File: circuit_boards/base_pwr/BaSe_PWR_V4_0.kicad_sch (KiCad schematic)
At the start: 105 parts, among them J1 12VDC In, J1 USB_C_Receptacle, J11 Conn_01x07_Pin, J2 USB_B_Micro, J3 USB3_A, J4 Screw_Terminal_01x04, J5 MOTOR, J5 Screw_Terminal_01x03, J7 USB3_B_Micro, P1 USB_C_Plug, Q2 BSS214NW, Q3 BSS214NW, Q4 BSS214NW, Q5 BSS214NW, U2 AMS1117-3.3, U3 STM32F070RBTx, U4 LM2596S-5, U5 DRV8220, U6 AMS1117-3.3, Y1 32.768kHz, Y2 8MHz

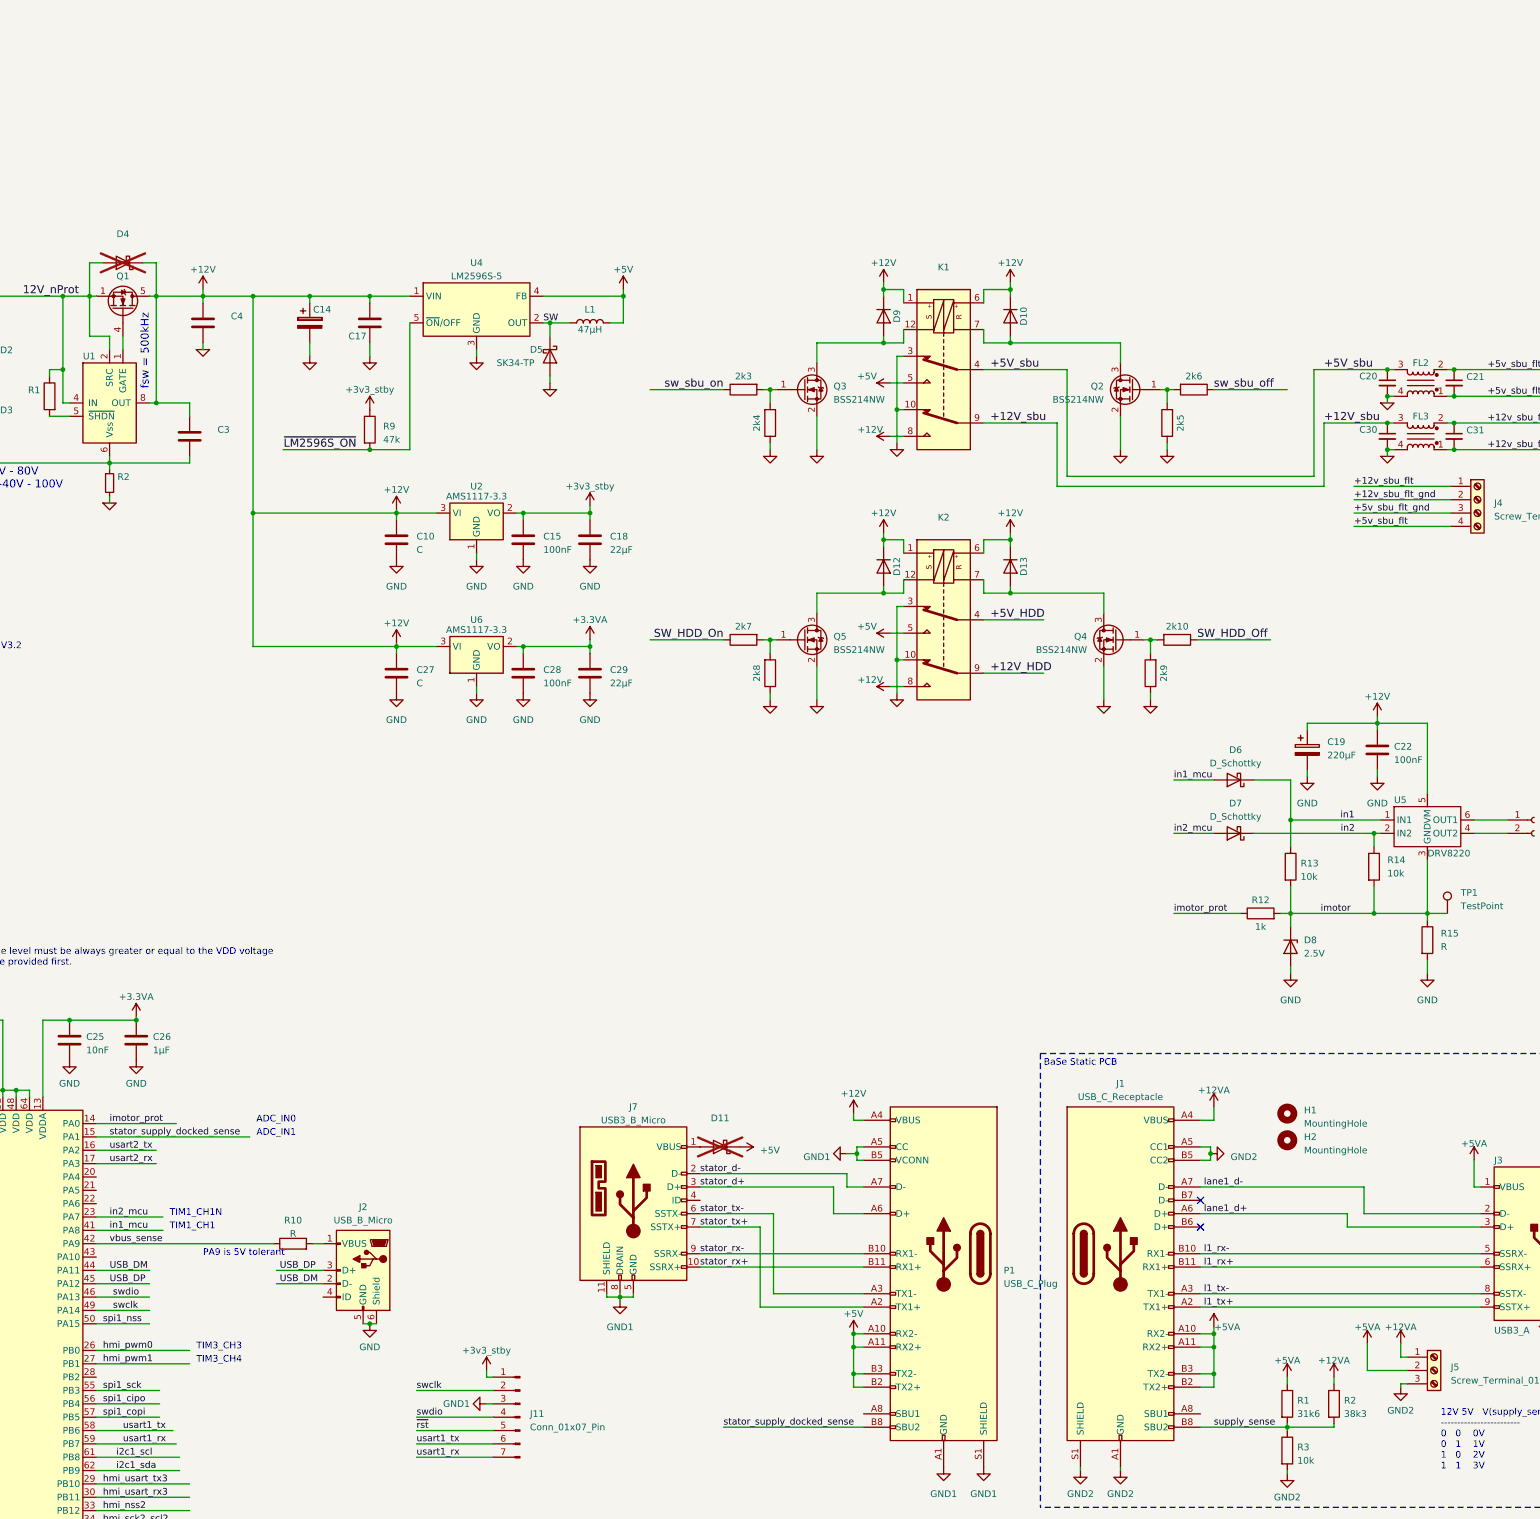
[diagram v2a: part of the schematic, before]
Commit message: BaSe PWR V4.0: more layout sketches
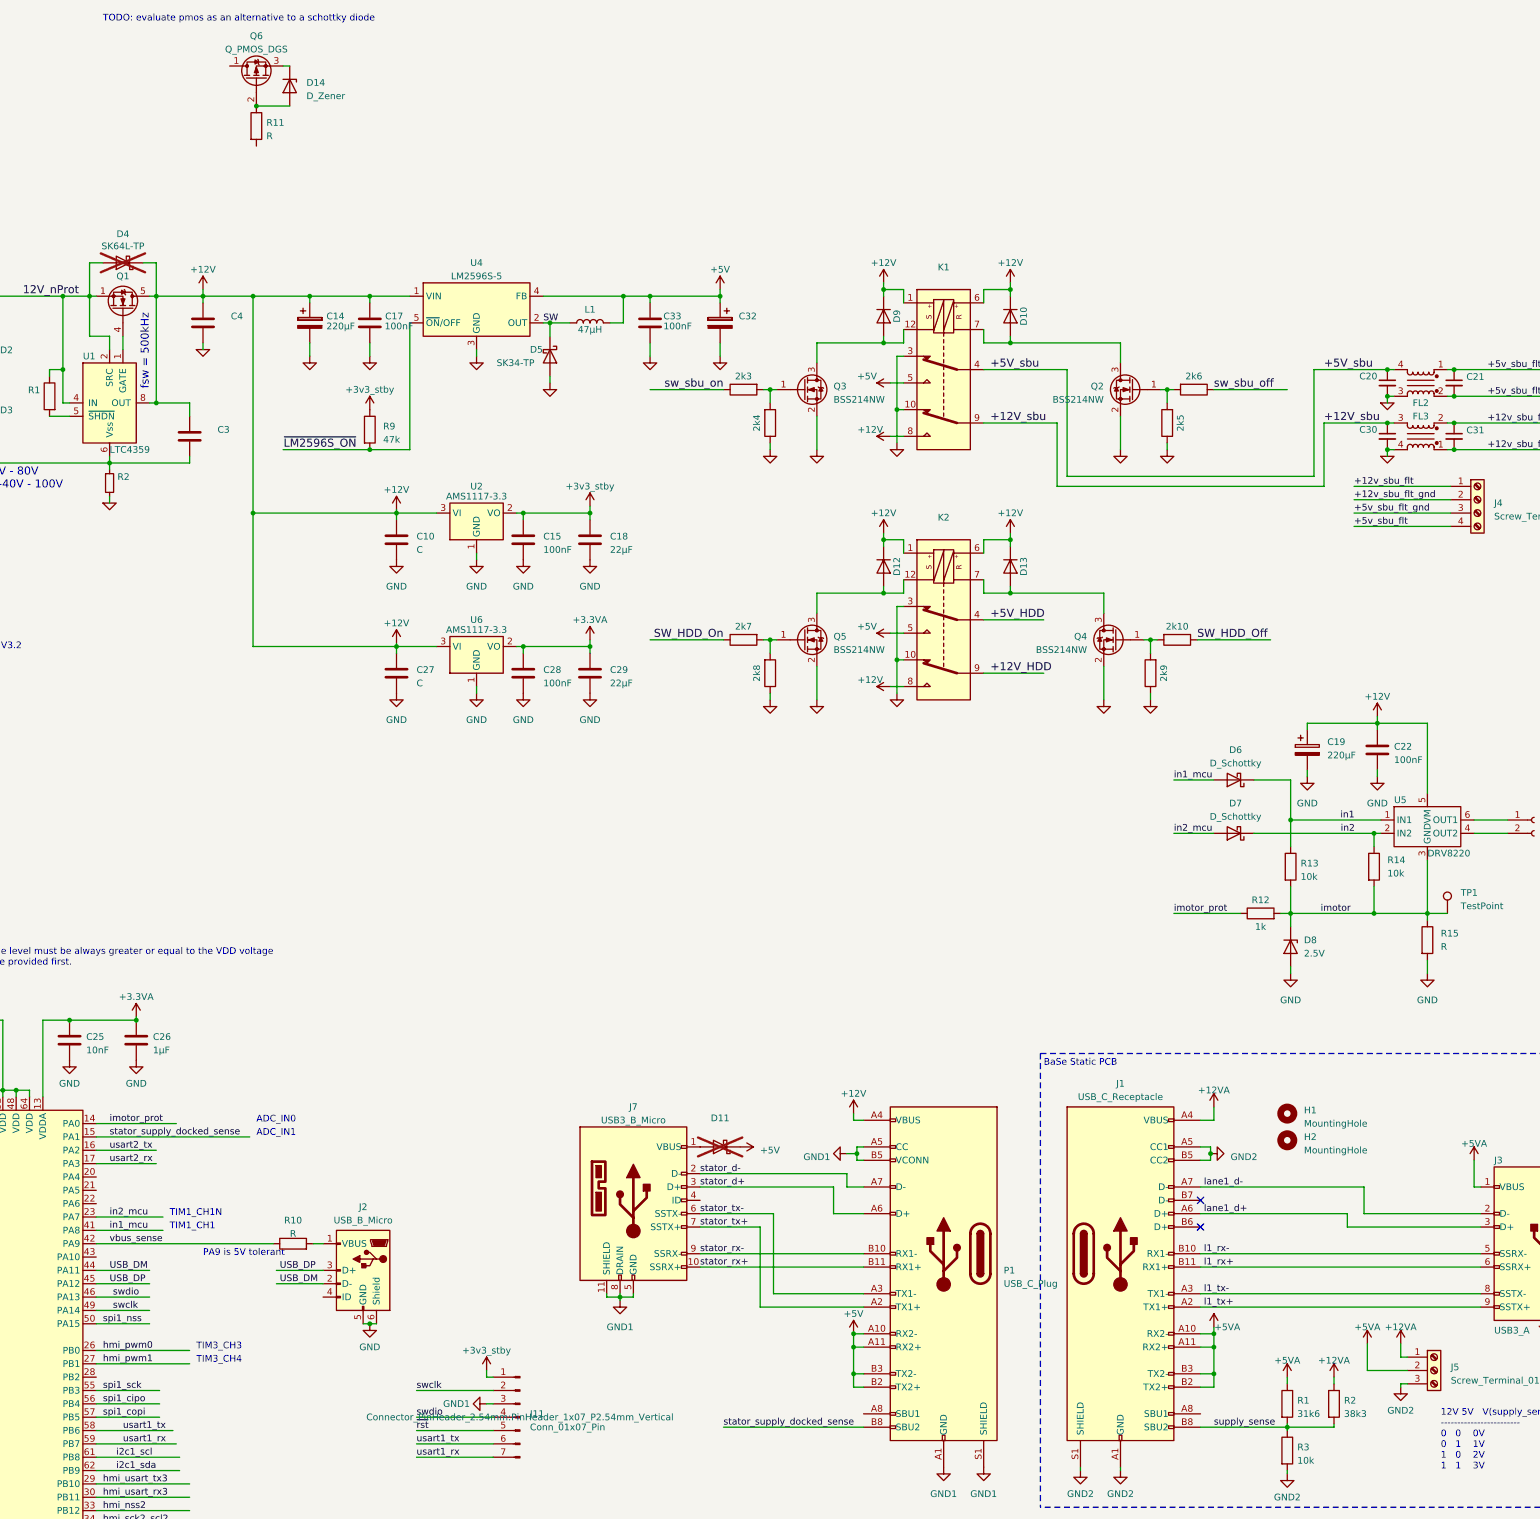
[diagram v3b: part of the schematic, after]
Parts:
- added C32: ~, Capacitor_SMD:C_0603_1608Metric_Pad1.08x0.95mm_HandSolder, symbol Waberinator_rev1-rescue:CP
- added C33: 100nF, Capacitor_SMD:C_0603_1608Metric_Pad1.08x0.95mm_HandSolder, symbol Waberinator_rev1-rescue:C
- added D14: D_Zener, symbol Device:D_Zener
- added Q6: Q_PMOS_DGS, symbol Device:Q_PMOS_DGS
- added R11: R, symbol Device:R
- C14: value ~ -> 220µF
- C17: value ~ -> 100nF
- D1: footprint (none) -> Diode_SMD:D_SOD-128
- D4: value ~ -> SK64L-TP
- F1: footprint (none) -> Fuse:Fuse_2512_6332Metric_Pad1.52x3.35mm_HandSolder; SPN F3147CT-ND -> (none); digikey (none) -> F3147CT-ND
- J1: footprint (none) -> Connector_JST:JST_XA_S02B-XASK-1N-BN_1x02_P2.50mm_Horizontal
- J11: footprint (none) -> Connector_PinHeader_2.54mm:PinHeader_1x07_P2.54mm_Vertical
- U1: value ~ -> LTC4359
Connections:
- net +5V: now also C32.1, C33.2
- net +5V_sbu: now also FL2.4; no longer FL2.3
- net +5v_sbu_flt: now also FL2.1; no longer FL2.2
- net +5v_sbu_flt_gnd: now also FL2.2; no longer FL2.1
- net GND: now also FL2.3, C32.2, C33.1; no longer FL2.4
- new net: D14.1 (K), Q6.3 (S)
- new net: D14.2 (A), Q6.2 (G), R11.1
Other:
- note added: "TODO: evaluate pmos as an alternative to a schottky diode"
- moved on the sheet: FL2

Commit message: BaSe PWR V4.0: design reverse polarity protection
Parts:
- removed C3, C4: ~, Capacitor_SMD:C_0603_1608Metric_Pad1.08x0.95mm_HandSolder, symbol BackupServer-rescue:C-BackupServer-rescue
- removed C32: ~, Capacitor_SMD:C_0603_1608Metric_Pad1.08x0.95mm_HandSolder, symbol Waberinator_rev1-rescue:CP
- removed D2, D3: ~, symbol Device:D_Zener
- removed D4: SK64L-TP, symbol Device:D_Schottky
- removed Q1: ~, symbol Transistor_FET:BSC028N06LS3
- removed R1: ~, Resistor_SMD:R_0603_1608Metric_Pad0.98x0.95mm_HandSolder, symbol BackupServer-rescue:R-BackupServer-rescue
- removed R2: ~, Resistor_SMD:R_0603_1608Metric_Pad0.98x0.95mm_HandSolder, symbol Device:R_Small
- removed U1: LTC4359, symbol Power_Management:LTC4359-MS8
- added C3: 220µF, Capacitor_SMD:C_Elec_10x10.2, symbol Waberinator_rev1-rescue:CP
- added R1: 100k, symbol Device:R
- C14: footprint Capacitor_SMD:C_0603_1608Metric_Pad1.08x0.95mm_HandSolder -> Capacitor_SMD:C_Elec_10x10.2
- C19: footprint Capacitor_SMD:C_Elec_6.3x7.7 -> Capacitor_SMD:C_Elec_10x10.2
- D1: value ~ -> 824501121
- D14: now not fitted
- J5: footprint Connector_PinHeader_2.54mm:PinHeader_1x02_P2.54mm_Vertical -> Connector_JST:JST_XA_S02B-XASK-1N-BN_1x02_P2.50mm_Horizontal
- Q6: value Q_PMOS_DGS -> AOSP21321; footprint (none) -> Package_SO:SO-8_3.9x4.9mm_P1.27mm
- R11: value R -> 100
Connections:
- net +12V: now also D14.1 (K), Q6.1 (S), Q6.2 (S), Q6.3 (S), R1.1
- net +3V3_STBY: no longer R9.1
- net +5V: now also C3.1
- net 12V_nProt: now also Q6.5 (D), Q6.6 (D), Q6.7 (D), Q6.8 (D)
- net GND: now also R11.2, R9.2, C3.2
- net ~{LM2596S_ON}: now also R9.1; no longer R9.2
- net at D14.2 (A), R11.1: now also Q6.4 (G), R1.2; no longer Q6.2 (G)
- net at U5.4 (OUT2): now also J5.1 (Pin_1); no longer J5.2 (Pin_2)
- net at U5.6 (OUT1): now also J5.2 (Pin_2); no longer J5.1 (Pin_1)
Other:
- note added: "5A flow at about 16V"
- note removed: "Operating: 4V - 80V Withstands: -40V - 100V"
- note removed: "TODO: evaluate pmos as an alternative to a schottky diode"
- note removed: "fsw = 500kHz"
- moved on the sheet: C1, C2, D1, FL1, J1, R11, R9

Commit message: BaSe PWR V4.0: settle on rough component distribution
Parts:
- removed C20, C21, C30, C31: ~, Capacitor_SMD:C_0603_1608Metric_Pad1.08x0.95mm_HandSolder, symbol Device:C_Small
- removed FL2, FL3: ~, g7_emi:CMC_Laird_CM2021Y330R-10, symbol Device:EMI_Filter_LL_1423
- removed J4: Screw_Terminal_01x04, TerminalBlock_Phoenix:TerminalBlock_Phoenix_MKDS-1,5-4_1x04_P5.00mm_Horizontal, symbol Connector:Screw_Terminal_01x04
- added J10: Conn_01x04_Socket, Connector_JST:JST_XH_B4B-XH-A_1x04_P2.50mm_Vertical, symbol Connector:Conn_01x04_Socket
- J1, J5: footprint Connector_JST:JST_XA_S02B-XASK-1N-BN_1x02_P2.50mm_Horizontal -> Connector_JST:JST_XH_B2B-XH-A_1x02_P2.50mm_Vertical
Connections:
- net +12V_sbu: now also J10.1 (Pin_1)
- net +5V_sbu: now also J10.4 (Pin_4)
- net GND: now also J10.2 (Pin_2), J10.3 (Pin_3)
- net USB_DM renamed USB_D-
- net USB_DP renamed USB_D+

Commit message: BaSe PWR V4.0: split pcbs so all connectors can face far end.
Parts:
- removed C7, C8: 4.3pF, Capacitor_SMD:C_0603_1608Metric_Pad1.08x0.95mm_HandSolder, symbol Device:C
- removed J5: Screw_Terminal_01x03, TerminalBlock_Phoenix:TerminalBlock_Phoenix_MKDS-1,5-3_1x03_P5.00mm_Horizontal, symbol Connector:Screw_Terminal_01x03
- removed R4: R, Resistor_SMD:R_0603_1608Metric_Pad0.98x0.95mm_HandSolder, symbol Device:R
- removed Y1: 32.768kHz, Crystal:Crystal_SMD_Abracon_ABS25-4Pin_8.0x3.8mm, symbol Device:Crystal
- added H1, H2: MountingHole, MountingHole:MountingHole_2.7mm_M2.5_DIN965, symbol Mechanical:MountingHole
- added J12: Conn_02x06_Odd_Even, Connector_PinHeader_2.54mm:PinHeader_2x06_P2.54mm_Vertical, symbol Connector_Generic:Conn_02x06_Odd_Even
- added J13: Conn_01x04_Socket, Connector_JST:JST_XH_B4B-XH-A_1x04_P2.50mm_Vertical, symbol Connector:Conn_01x04_Socket
- added J4: Conn_02x06_Odd_Even, Connector_PinSocket_2.54mm:PinSocket_2x06_P2.54mm_Vertical, symbol Connector_Generic:Conn_02x06_Odd_Even
- C10, C27: value C -> 100nF
- H1, H2: footprint MountingHole:MountingHole_3.2mm_M3_DIN965 -> MountingHole:MountingHole_2.7mm_M2.5_DIN965
- R1, R11: footprint (none) -> Resistor_SMD:R_0603_1608Metric_Pad0.98x0.95mm_HandSolder
- R6: value 33k -> 24,9k
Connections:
- net +12V: no longer P1.A4 (VBUS), P1.A9 (VBUS), P1.B4 (VBUS), P1.B9 (VBUS)
- net +12VA: now also J13.4 (Pin_4)
- net +12V_HDD: now also J4.5 (Pin_5), J4.6 (Pin_6)
- net +12V_sbu: now also J10.4 (Pin_4); no longer J10.1 (Pin_1)
- net +3V3_STBY: now also J4.12 (Pin_12)
- net +5V: no longer D11.1 (K), P1.A10 (RX2-), P1.A11 (RX2+), P1.B2 (TX2+), P1.B3 (TX2-)
- net +5VA: now also J13.1 (Pin_1)
- net +5V_HDD: now also J4.3 (Pin_3), J4.4 (Pin_4)
- net +5V_sbu: now also J10.1 (Pin_1); no longer J10.4 (Pin_4)
- net GND: now also J4.1 (Pin_1), J4.2 (Pin_2), J4.7 (Pin_7), J4.8 (Pin_8)
- net GND1: now also J12.1 (Pin_1), J12.2 (Pin_2), J12.7 (Pin_7), J12.8 (Pin_8); no longer P1.A5 (CC), P1.B5 (VCONN)
- net GND2: now also J13.2 (Pin_2), J13.3 (Pin_3); no longer J1.A5 (CC1), J1.B5 (CC2)
- net i2c1_scl: now also J4.9 (Pin_9)
- net i2c1_sda: now also J4.10 (Pin_10)
- net supply_sense: now also J1.A5 (CC1); no longer J1.B8 (SBU2)
- net aux_i2c_scl: now reaches P1.A8 (SBU1)
- net stator_supply_docked_sense renamed aux_i2c_sda
- net aux_i2c_sda: no longer U3.15 (PA1)
- new net +12V_HDD_: J12.5 (Pin_5), J12.6 (Pin_6), P1.A4 (VBUS), P1.A9 (VBUS), P1.B4 (VBUS), P1.B9 (VBUS)
- new net +5V_HDD_: D11.1 (K), J12.3 (Pin_3), J12.4 (Pin_4), P1.A10 (RX2-), P1.A11 (RX2+), P1.B2 (TX2+), P1.B3 (TX2-)
- new net aux_3v3: J12.12 (Pin_12), P1.B5 (VCONN)
- new net i2c_scl: J12.9 (Pin_9)
- new net i2c_sda: J12.10 (Pin_10)
- new net stator_supply_sense: J12.11 (Pin_11), J4.11 (Pin_11), P1.A5 (CC), U3.15 (PA1)
- no-connect marks 3 -> 8
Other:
- note added: "16V map to 3,2V"
- note added: "BaSe USB Adapter Carriage"
- note added: "todo: do I need the crystals?"
- moved on the sheet: H1, H2, J11, R1, R2, R3

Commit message: BaSe_PWR_V4_0: add last footprints, position components
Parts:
- removed C18, C29: 22µF, symbol Device:C
- removed C24: 4.7µF, symbol Device:C
- removed D14: D_Zener, symbol Device:D_Zener
- added C1: 4.7µF, Capacitor_THT:C_Radial_D4.0mm_H7.0mm_P1.50mm, symbol Waberinator_rev1-rescue:CP
- added C20, C21: 22µF, Capacitor_THT:C_Radial_D5.0mm_H11.0mm_P2.00mm, symbol Waberinator_rev1-rescue:CP
- added D11: D_Schottky, Diode_SMD:D_SOD-123, symbol Device:D_Schottky
- added H1 (x3): MountingHole, MountingHole:MountingHole_2.7mm_M2.5_DIN965, symbol Mechanical:MountingHole
- added R1: 100, Resistor_SMD:R_0603_1608Metric_Pad0.98x0.95mm_HandSolder, symbol BackupServer-rescue:R-BackupServer-rescue
- added R19: 100, Resistor_SMD:R_0603_1608Metric_Pad0.98x0.95mm_HandSolder, symbol Device:R
- D3: renamed from D11; footprint (none) -> Diode_SMD:D_SOD-123
- J2: renamed from J3; footprint (none) -> Connector_PinHeader_2.54mm:PinHeader_1x18_P2.54mm_Vertical
- R2: renamed from 2k1; value ~ -> 100
- renumbered 2k3 to 2k1, 2k7 to 2k2, 2k4 to 2k3, 2k8 to 2k4, 2k9 to 2k5, 2k5 to 2k6, 2k10 to 2k7, 2k6 to 2k8, C11 to C10, C23 to C11, C25 to C12, C26 to C13, C17 to C15, C10 to C16, C27 to C17, C15 to C18, C28 to C19, C5 to C2, C33 to C22, C3 to C23, C19 to C24, C22 to C25, C6 to C3, C9 to C4, C1 to C5, C12 to C6, C2 to C7, C13 to C8, C16 to C9, D8 to D10, D5 to D2, D9 to D4, D12 to D5, D10 to D6, D13 to D7, D6 to D8, D7 to D9, J13 to J10, J5 to J11, J2 to J3, J11 to J4, J4 to J5, J12 to J7, J10 to J9, Q6 to Q1, Q3 to Q2, Q5 to Q3, Q2 to Q5, R9 to R11, R14 to R16, R15 to R18, R7 to R4, R8 to R5, R5 to R6, R6 to R7, R11 to R8, R1 to R9, U3 to U1, U4 to U2, U2 to U3, U6 to U4, Y2 to Y1
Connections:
- net +3.3VA: now also C21.1
- net +3V3_STBY: now also C1.1, C20.1
- net 12vin_meas: now also U1.20 (PA4), R19.2; no longer C10.1, R6.1, R7.2
- net Dis_PWM: now also R1.2; no longer U1.26 (PB0)
- net GND: now also C1.2, C20.2, C21.2, D11.2 (A)
- new net: C10.1, D11.1 (K), R19.1, R6.1, R7.2
- new net hmi_pwm0: R1.1, U1.26 (PB0)
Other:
- moved on the sheet: H1, Q1, R8, R9

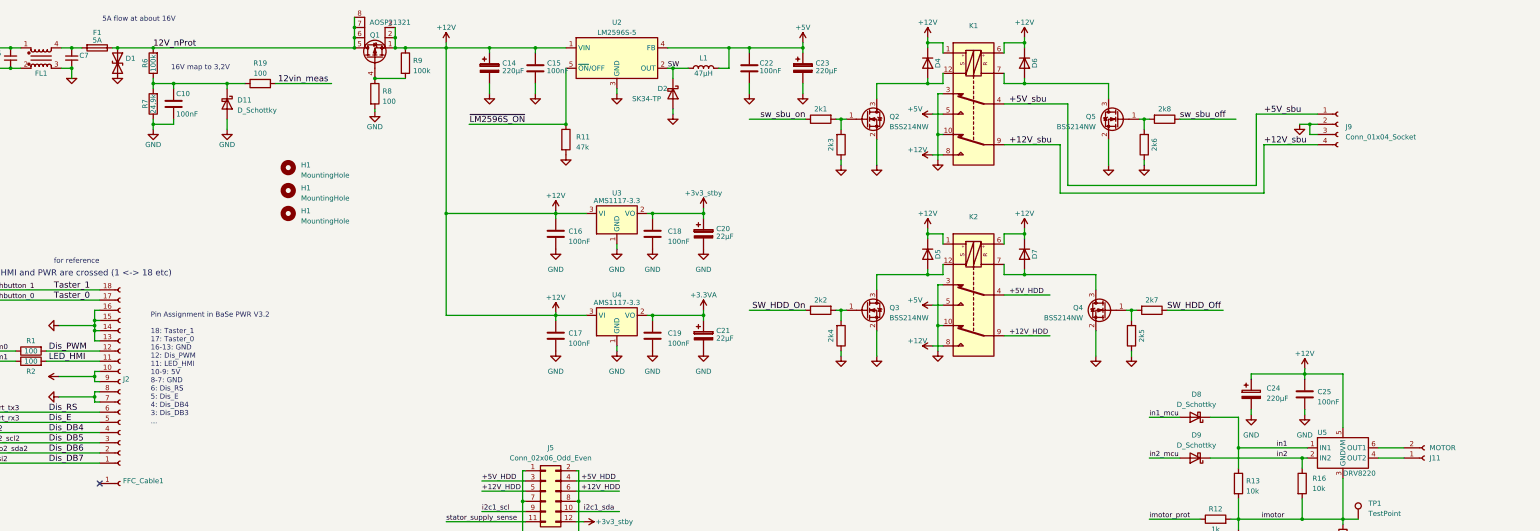
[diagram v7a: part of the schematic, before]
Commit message: BaSe PWR V4.0: add stub for power backup based on 9V block
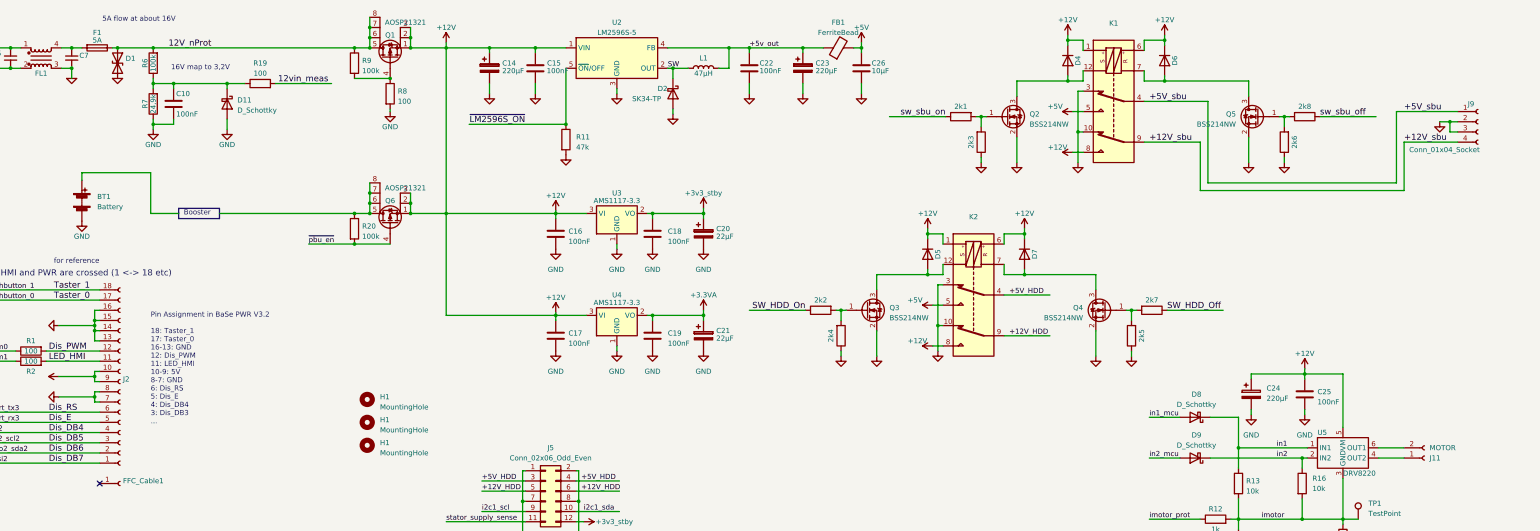
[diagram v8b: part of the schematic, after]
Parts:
- added BT1: Battery, symbol Device:Battery
- added C26: 10µF, Capacitor_SMD:C_1206_3216Metric_Pad1.33x1.80mm_HandSolder, symbol Waberinator_rev1-rescue:C
- added FB1: FerriteBead, Capacitor_SMD:C_1206_3216Metric_Pad1.33x1.80mm_HandSolder, symbol Device:FerriteBead
- added Q6: AOSP21321, Package_SO:SO-8_3.9x4.9mm_P1.27mm, symbol Device:Q_PMOS_DGS
- added R20: 100k, Resistor_SMD:R_0603_1608Metric_Pad0.98x0.95mm_HandSolder, symbol Device:R
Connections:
- net +12V: now also Q6.1 (S), Q6.2 (S), Q6.3 (S); no longer R9.1
- net +5V: now also C26.2, FB1.2; no longer C22.2, C23.1, L1.2, U2.4 (FB)
- net 12V_nProt: now also R9.1
- net GND: now also BT1.2 (-), C26.1
- new net: Q6.5 (D), Q6.6 (D), Q6.7 (D), Q6.8 (D), R20.1
- new net +5v_out: C22.2, C23.1, FB1.1, L1.2, U2.4 (FB)
- new net ~{pbu_en}: Q6.4 (G), R20.2
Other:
- note added: "Booster"
- moved on the sheet: 2k1, 2k3, 2k6, 2k8, D4, D6, H1, J9, K1, Q1, Q2, Q5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
